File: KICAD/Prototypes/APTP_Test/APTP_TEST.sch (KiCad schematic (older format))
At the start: 1 part

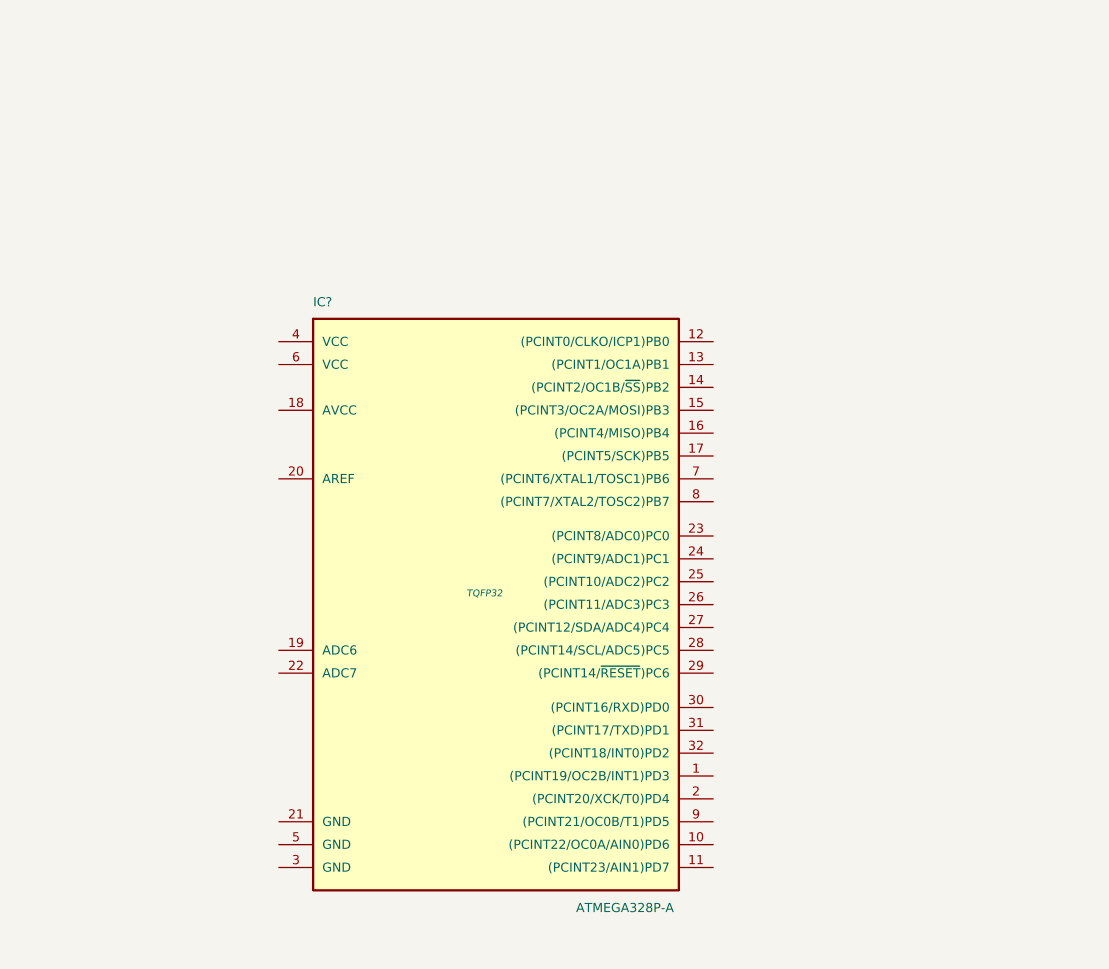
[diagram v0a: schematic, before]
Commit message: Added an experiment + APA test board
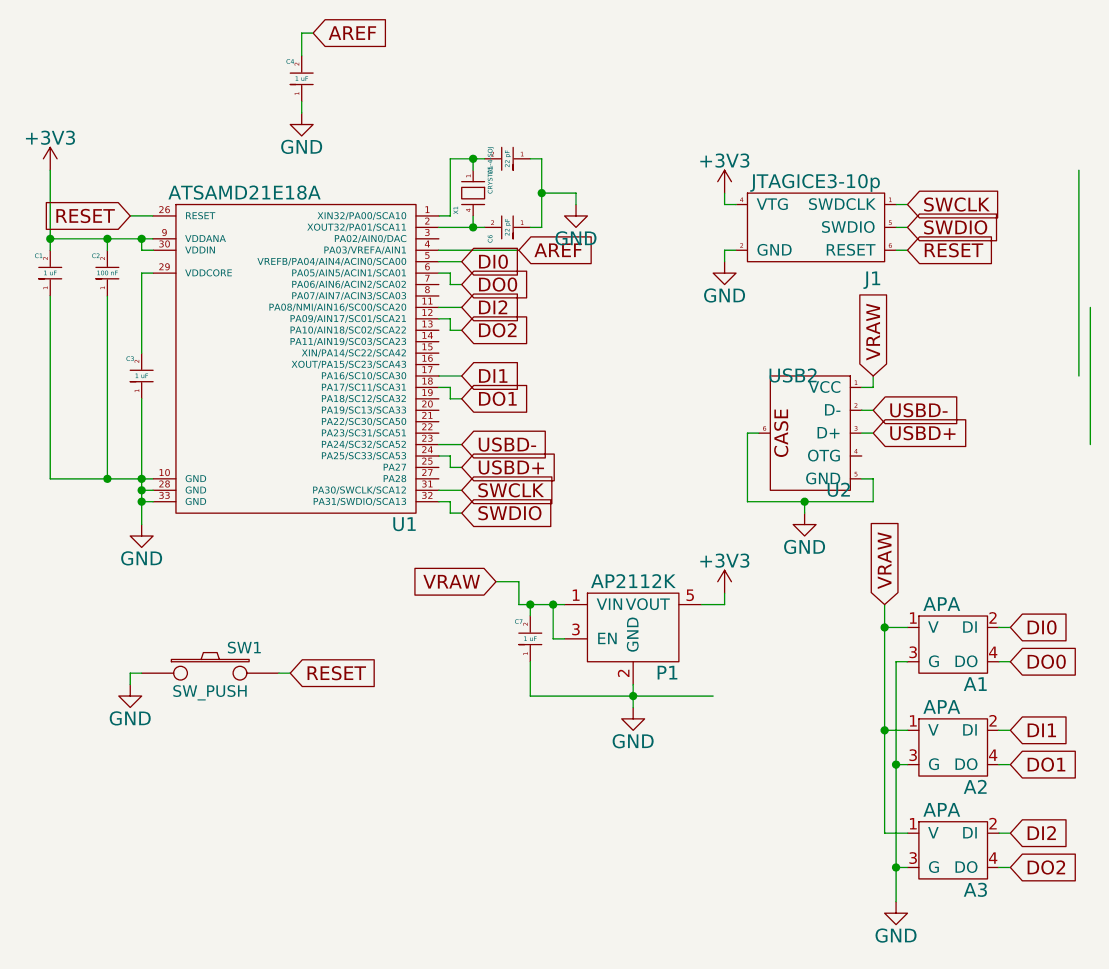
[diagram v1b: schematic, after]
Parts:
- removed IC?: ATMEGA328P-A, TQFP32, symbol ATMEGA328P-A
- added A1, A2, A3: APA, _Fab_Footprint:SMD-Header-2x2, symbol APA
- added C1, C3, C4, C7: 1 uF, _Fab_Footprint:CAP_1206_FAB, symbol CAP
- added C2: 100 nF, _Fab_Footprint:CAP_1206_FAB, symbol CAP
- added C5, C6: 22 pF, _Fab_Footprint:CAP_1206_FAB, symbol CAP
- added J1: JTAGICE3-10p, _Fab_Footprint:SMD-Header-3x2, symbol JTAGICE3-10p
- added P1: AP2112K, _Fab_Footprint:SOT-23-5, symbol AP2112K
- added SW1: SW_PUSH, _Fab_Footprint:Switch-Tactile-B3SN-3112P, symbol SW_PUSH
- added U1: ATSAMD21E18A, _Fab_Footprint:TQFP-32-Fab, symbol ATSAMD21E18A
- added U2: USB2, _Fab_Footprint:USBMINIB2.0, symbol USB2
- added X1: CRYSTAL-4-SOJ, _Fab_Footprint:4-SOJ, symbol CRYSTAL-4-SOJ
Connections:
- net labels added: +3V3, AREF, DI0, DI1, DI2, DO0, DO1, DO2, GND, RESET, SWCLK, SWDIO, USBD+, USBD-, VRAW
- wire segments 0 -> 96
